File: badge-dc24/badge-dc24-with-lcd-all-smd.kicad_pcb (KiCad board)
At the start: 2 copper layers, 30 parts, among them U1 ESP-12E, U2 TSOP38238, U3 74HC595, U4 MC78L05ACH

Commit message: Changed git commit sha on board
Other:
- board text added: "f79562f55e8a6107247b5f8850298d5d49aaa443"
- board text removed: "73950de5c7766f8ae4fb76bc7ecf4b83f05361bd"
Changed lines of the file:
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@@
     (links 69)
     (no_connects 0)
-    (area 0 0 0 0)
+    (area 49.57 58.46 152.36 130.77)
     (thickness 1.6)
     (drawings 9)
@@
     (effects (font (size 1.5 1.5) (thickness 0.3)))
   )
-  (gr_text 73950de5c7766f8ae4fb76bc7ecf4b83f05361bd (at 96.1644 123.4948) (layer F.Cu)
+  (gr_text f79562f55e8a6107247b5f8850298d5d49aaa443 (at 96.1644 123.4948) (layer F.Cu)
     (effects (font (size 1.5 1.5) (thickness 0.3)))
   )

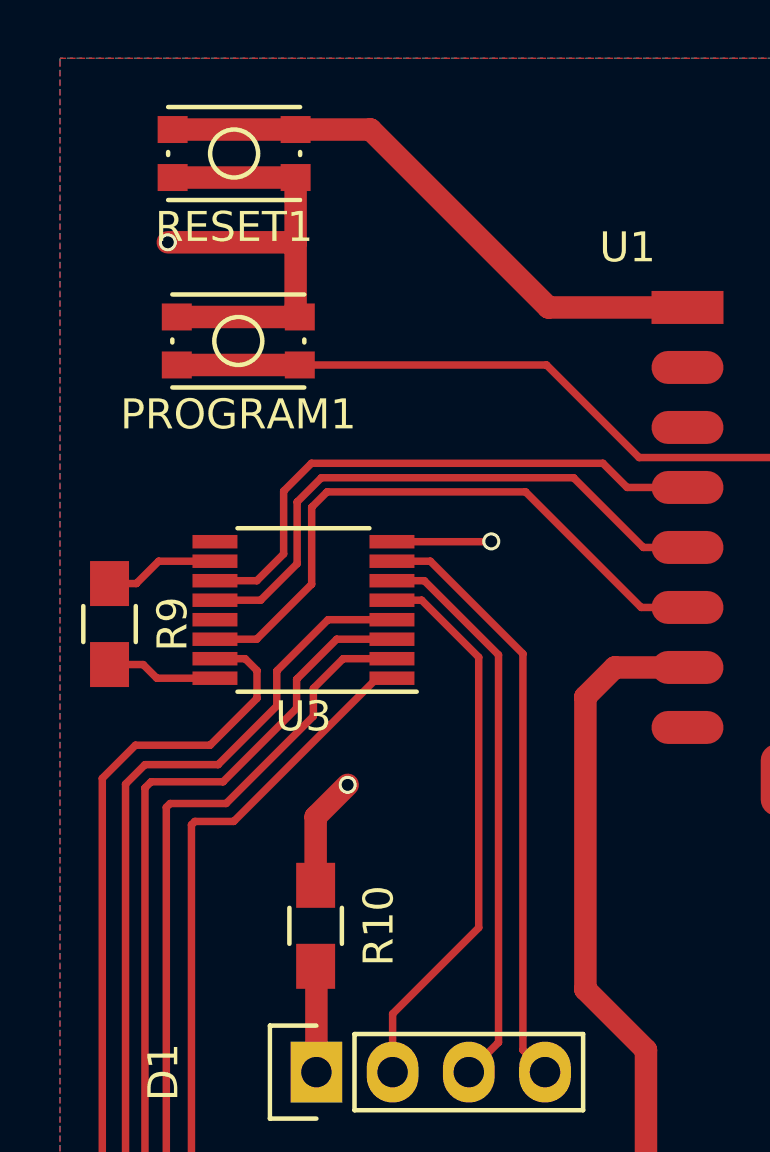
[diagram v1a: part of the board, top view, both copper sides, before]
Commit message: More SMD components
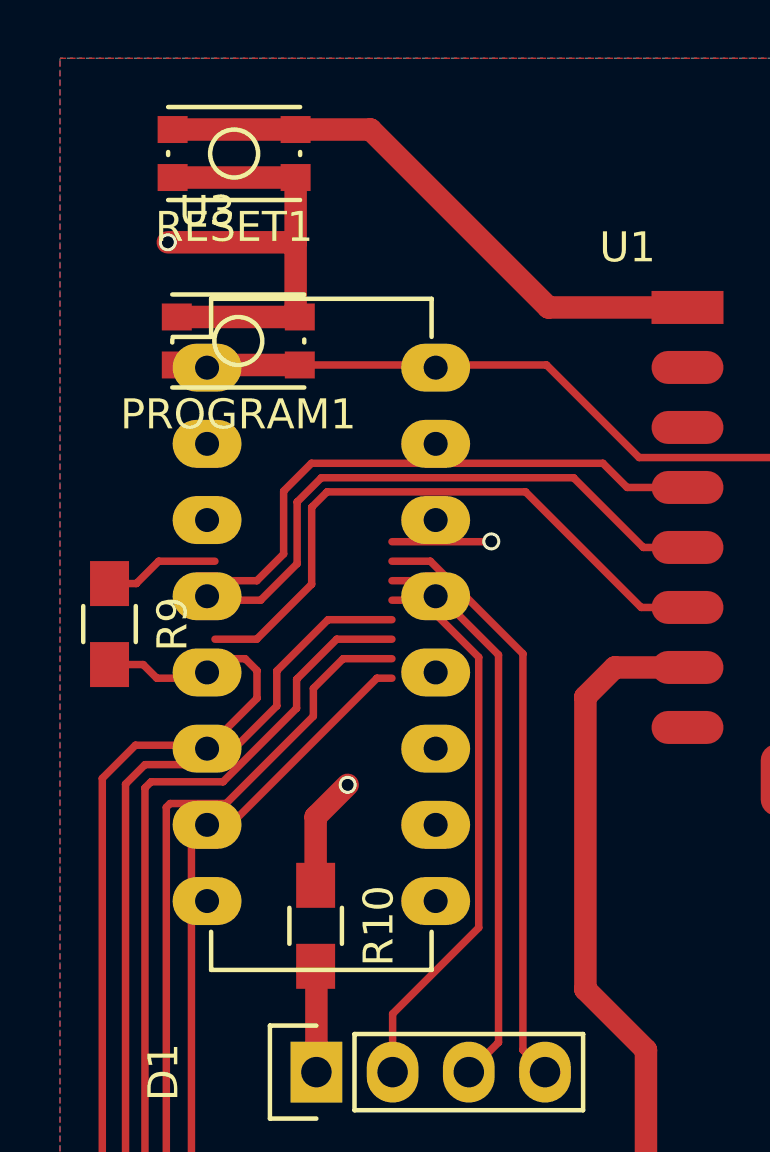
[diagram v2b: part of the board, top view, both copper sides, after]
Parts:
- U3: footprint Housings_SSOP:TSSOP-16_4.4x5mm_Pitch0.65mm -> Housings_DIP:DIP-16_W7.62mm_LongPads
- moved U3 8.69 mm to (59.7, 74.3), turned to 0 degrees
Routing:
- net Net-(D1-Pad4): track 19.9 -> 51.6 mm, vias 0 -> 1
- net Net-(L4-Pad1): track 25.2 -> 3.42 mm, vias 1 -> 0
- net Net-(D1-Pad3): track 18.9 -> 30.9 mm
- net Net-(L3-Pad1): track 31.0 -> 21.1 mm
- net Net-(U3-Pad13): track 0.00 -> 8.26 mm
- net Net-(L5-Pad1): track 41.6 -> 34.4 mm
- net Net-(L1-Pad1): track 40.9 -> 35.9 mm
- net (no net): track 0.00 -> 3.32 mm, vias 0 -> 1
- net GND: track 62.2 -> 58.8 mm, vias 4 -> 3
- net Net-(U1-Pad5): track 19.6 -> 16.4 mm
- net Net-(U1-Pad4): track 18.9 -> 16.3 mm
- net +3V3: track 13.8 -> 11.9 mm

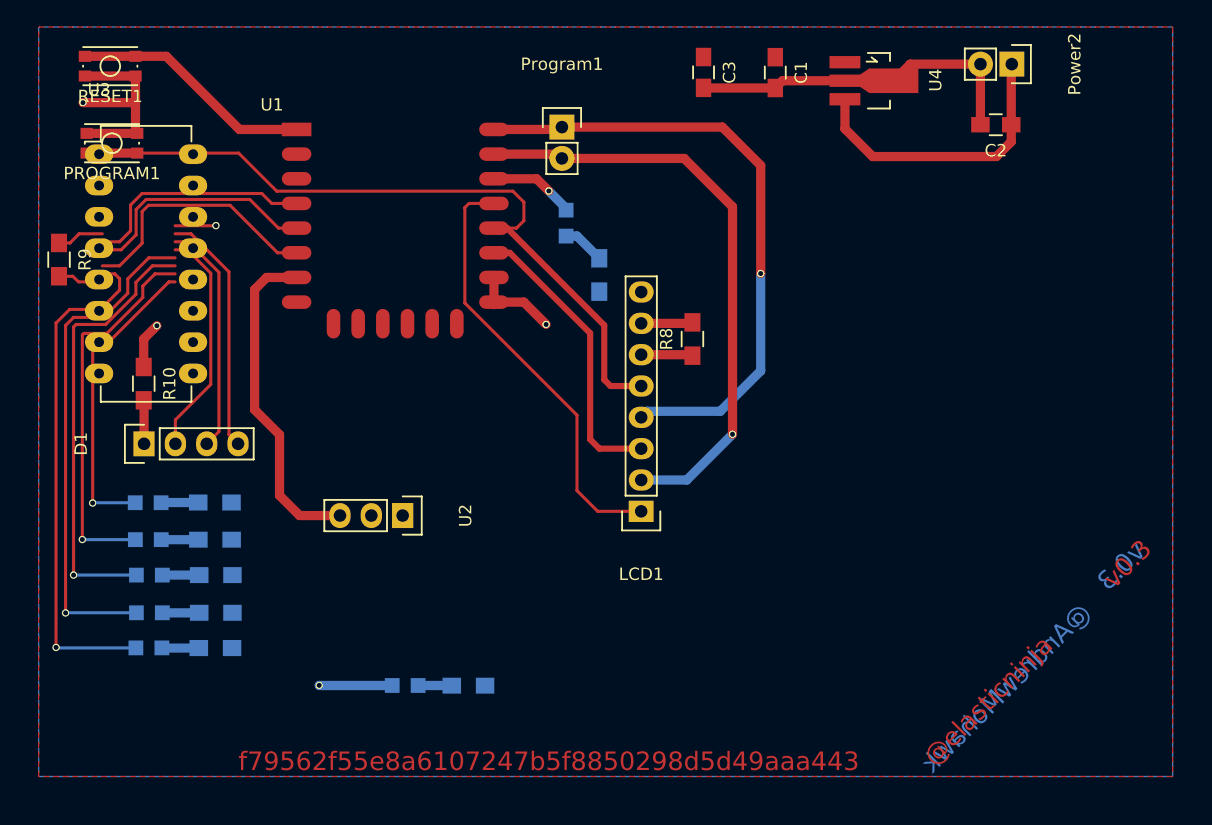
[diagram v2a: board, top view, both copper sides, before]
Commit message: v0.3 with SMD
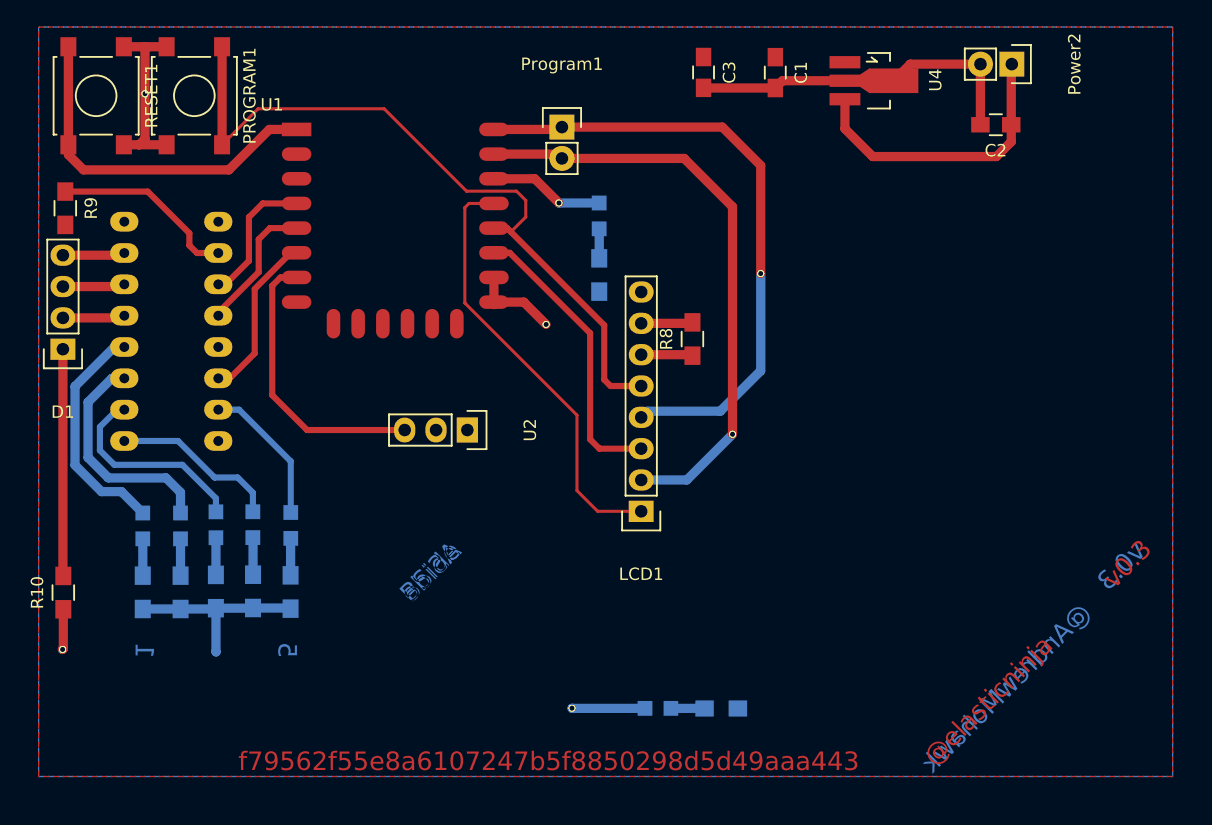
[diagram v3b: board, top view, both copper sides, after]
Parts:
- PROGRAM1, RESET1: footprint Buttons_Switches_SMD:SW_SPST_KMR2 -> Buttons_Switches_SMD:SW_SPST_B3S-1000
- U3: moved to B.Cu
- moved U3 23.3 mm to (61.7, 97.5)
- moved Power1 20.6 mm to (105.0, 119.2)
- moved R1 20.6 mm to (110.1, 119.2)
- moved R10 18.2 mm to (56.8, 109.8), turned to 90 degrees
- moved L5 15.2 mm to (75.2, 104.4), turned to 270 degrees
- moved D1 10.1 mm to (56.8, 90.1), turned to 180 degrees
- moved U2 8.69 mm to (89.6, 96.6)
- moved L4 8.68 mm to (72.2, 104.3), turned to 270 degrees
- moved R4 7.84 mm to (72.2, 109.7), turned to 270 degrees
- moved PROGRAM1 7.71 mm to (67.4, 69.5), turned to 270 degrees
- moved R3 7.60 mm to (75.2, 109.8), turned to 270 degrees
- moved L1 7.07 mm to (63.2, 104.4), turned to 270 degrees
- moved R7 6.15 mm to (63.2, 109.8), turned to 270 degrees
- moved L3 5.61 mm to (69.2, 104.3), turned to 270 degrees
- moved L2 4.72 mm to (66.3, 104.4), turned to 270 degrees
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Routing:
- net Net-(D1-Pad4): track 51.6 -> 5.05 mm, vias 1 -> 0
- net Net-(D1-Pad3): track 30.9 -> 5.05 mm
- net Net-(L5-Pad1): track 34.4 -> 12.7 mm, vias 1 -> 0
- net Net-(L2-Pad1): track 36.1 -> 18.6 mm, vias 1 -> 0
- net Net-(L1-Pad1): track 35.9 -> 18.8 mm, vias 1 -> 0
- net Net-(D1-Pad1): track 3.54 -> 18.4 mm
- net GND: track 58.8 -> 72.4 mm
- net Net-(D1-Pad2): track 18.5 -> 5.05 mm
- net Net-(R9-Pad1): track 3.82 -> 15.0 mm
- net Net-(L4-Pad1): track 3.42 -> 13.7 mm
- net Net-(RESET1-Pad2): track 19.6 -> 29.9 mm
- net Net-(U3-Pad13): track 8.26 -> 0.00 mm
- net Net-(U1-Pad6): track 21.8 -> 14.6 mm
- net Net-(U1-Pad5): track 16.4 -> 11.7 mm
- net Net-(L3-Pad1): track 21.1 -> 16.6 mm, vias 1 -> 0
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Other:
- board text added: "1"
- board text added: "5"
- board text added: "ASide"
- board text added: "BSide"
